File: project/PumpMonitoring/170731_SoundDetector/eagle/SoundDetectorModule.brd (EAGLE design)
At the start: 46 x 22 mm, 32 parts, among them CN1 JST-PH-K*, IC1 LMV324

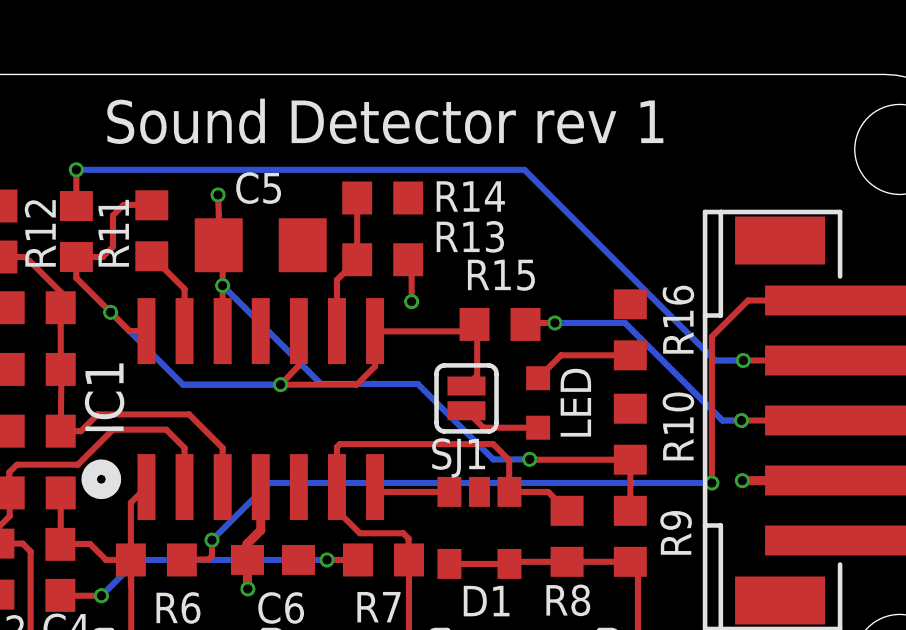
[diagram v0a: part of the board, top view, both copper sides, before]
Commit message: update sound detector module
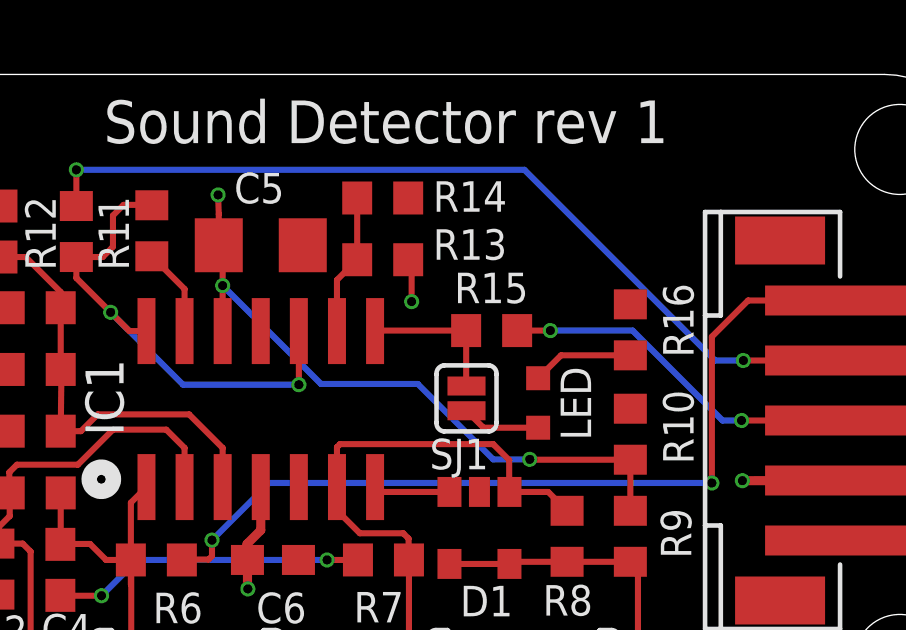
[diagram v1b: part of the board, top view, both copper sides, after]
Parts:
- moved R15 0.35 mm to (29.9, 13.5)
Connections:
- new net N$16: IC1.8, R15.1, SJ1.2
- net AMPENV: no longer IC1.8, R15.1, SJ1.2
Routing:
- net AMPENV: track 26.6 -> 16.7 mm
- net N$16: track 0.00 -> 4.91 mm
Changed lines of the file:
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@@
 <layer number="17" name="Pads" color="2" fill="1" visible="yes" active="yes"/>
 <layer number="18" name="Vias" color="2" fill="1" visible="yes" active="yes"/>
-<layer number="19" name="Unrouted" color="6" fill="1" visible="no" active="yes"/>
+<layer number="19" name="Unrouted" color="6" fill="1" visible="yes" active="yes"/>
 <layer number="20" name="Dimension" color="15" fill="1" visible="yes" active="yes"/>
 <layer number="21" name="tPlace" color="7" fill="1" visible="yes" active="yes"/>
@@
 </element>
 <element name="R13" library="rcl" package="R0603" value="100k" x="26.2636" y="15.8242" smashed="yes">
-<attribute name="NAME" x="27.94" y="16.0782" size="1.016" layer="21" font="vector" ratio="15"/>
+<attribute name="NAME" x="27.94" y="15.8242" size="1.016" layer="21" font="vector" ratio="15"/>
 </element>
 <element name="R14" library="rcl" package="R0603" value="3.3k" x="26.2636" y="17.8816" smashed="yes" rot="R180">
@@
 <attribute name="VALUE" x="27.2796" y="19.0246" size="0.4064" layer="27" font="vector" rot="R180"/>
 </element>
-<element name="R15" library="rcl" package="R0603" value="100" x="30.1752" y="13.6652" smashed="yes">
-<attribute name="NAME" x="28.9814" y="14.8082" size="1.016" layer="21" font="vector" ratio="15"/>
+<element name="R15" library="rcl" package="R0603" value="100" x="29.8958" y="13.462" smashed="yes">
+<attribute name="NAME" x="28.6512" y="14.3764" size="1.016" layer="21" font="vector" ratio="15"/>
 </element>
 <element name="R16" library="rcl" package="R0603" value="2.2k" x="34.5186" y="13.4874" smashed="yes" rot="R270">
@@
 <contactref element="R11" pad="2"/>
 <contactref element="R12" pad="1"/>
-<contactref element="R15" pad="1"/>
-<contactref element="SJ1" pad="2"/>
-<wire x1="29.3252" y1="13.6652" x2="29.4132" y2="13.5772" width="0.2032" layer="1"/>
-<contactref element="IC1" pad="10"/>
 <contactref element="IC1" pad="14"/>
-<contactref element="IC1" pad="8"/>
 <wire x1="16.0528" y1="15.914" x2="16.93" y2="15.914" width="0.2032" layer="1"/>
 <wire x1="16.93" y1="15.914" x2="17.272" y2="16.256" width="0.2032" layer="1"/>
@@
 <wire x1="16.0528" y1="15.2146" x2="16.0528" y2="15.914" width="0.2032" layer="1"/>
 <via x="17.1958" y="14.0716" extent="1-16" drill="0.3048"/>
-<via x="22.86" y="11.6586" extent="1-16" drill="0.3048"/>
-<wire x1="26.0096" y1="13.4458" x2="26.0096" y2="12.2682" width="0.2032" layer="1"/>
-<wire x1="26.0096" y1="12.2682" x2="25.4" y2="11.6586" width="0.2032" layer="1"/>
-<wire x1="25.4" y1="11.6586" x2="22.86" y2="11.6586" width="0.2032" layer="1"/>
-<wire x1="23.4696" y1="13.4458" x2="23.4696" y2="12.2936" width="0.2032" layer="1"/>
-<wire x1="23.4696" y1="12.2936" x2="22.86" y2="11.6586" width="0.2032" layer="1"/>
-<wire x1="22.86" y1="11.6586" x2="19.6088" y2="11.6586" width="0.2032" layer="16"/>
+<via x="23.4696" y="11.6586" extent="1-16" drill="0.3048"/>
+<wire x1="23.4696" y1="11.6586" x2="19.6088" y2="11.6586" width="0.2032" layer="16"/>
 <wire x1="19.6088" y1="11.6586" x2="17.1958" y2="14.0716" width="0.2032" layer="16"/>
-<wire x1="29.4132" y1="13.5772" x2="29.4132" y2="11.9689" width="0.2032" layer="1"/>
-<wire x1="29.4132" y1="11.9689" x2="29.0576" y2="11.6133" width="0.2032" layer="1"/>
-<wire x1="29.0576" y1="11.6133" x2="28.9759" y2="11.6133" width="0.2032" layer="1"/>
-<wire x1="26.0188" y1="13.4366" x2="26.0096" y2="13.4458" width="0.2032" layer="1"/>
-<wire x1="26.0188" y1="13.4366" x2="29.0966" y2="13.4366" width="0.2032" layer="1"/>
-<wire x1="29.0966" y1="13.4366" x2="29.3252" y2="13.6652" width="0.2032" layer="1"/>
+<contactref element="IC1" pad="10"/>
+<wire x1="23.4696" y1="13.4458" x2="23.4696" y2="11.6586" width="0.2032" layer="1"/>
 </signal>
 <signal name="N$15">
@@
 <contactref element="CN1" pad="3"/>
 <wire x1="41.7596" y1="10.4648" x2="38.227" y2="10.4648" width="0.2032" layer="1"/>
-<wire x1="31.076" y1="13.716" x2="31.0252" y2="13.6652" width="0.2032" layer="1"/>
 <via x="38.227" y="10.4648" extent="1-16" drill="0.3048"/>
-<wire x1="31.076" y1="13.716" x2="32.004" y2="13.716" width="0.2032" layer="1"/>
-<via x="32.004" y="13.716" extent="1-16" drill="0.3048"/>
-<wire x1="32.004" y1="13.716" x2="34.3408" y2="13.716" width="0.2032" layer="16"/>
-<wire x1="34.3408" y1="13.716" x2="37.592" y2="10.4648" width="0.2032" layer="16"/>
+<via x="31.8516" y="13.462" extent="1-16" drill="0.3048"/>
 <wire x1="37.592" y1="10.4648" x2="38.227" y2="10.4648" width="0.2032" layer="16"/>
+<wire x1="30.7458" y1="13.462" x2="31.8516" y2="13.462" width="0.2032" layer="1"/>
+<wire x1="31.8516" y1="13.462" x2="34.5948" y2="13.462" width="0.2032" layer="16"/>
+<wire x1="34.5948" y1="13.462" x2="37.592" y2="10.4648" width="0.2032" layer="16"/>
 </signal>
 <signal name="N$3">
@@
 <wire x1="9.144" y1="17.272" x2="9.652" y2="16.764" width="0.4064" layer="1"/>
 </signal>
+<signal name="N$16">
+<contactref element="R15" pad="1"/>
+<contactref element="SJ1" pad="2"/>
+<contactref element="IC1" pad="8"/>
+<wire x1="26.0188" y1="13.4366" x2="26.0096" y2="13.4458" width="0.3048" layer="1"/>
+<wire x1="29.0458" y1="13.462" x2="26.0258" y2="13.462" width="0.2032" layer="1"/>
+<wire x1="26.0258" y1="13.462" x2="26.0096" y2="13.4458" width="0.2032" layer="1"/>
+<wire x1="29.0458" y1="13.462" x2="29.0458" y2="11.6251" width="0.2032" layer="1"/>
+<wire x1="29.0458" y1="11.6251" x2="29.0576" y2="11.6133" width="0.2032" layer="1"/>
+</signal>
 </signals>
